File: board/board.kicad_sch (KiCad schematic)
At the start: 10 parts, among them U1 RP2040, U2 W25Q128JVS

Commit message: DVDD
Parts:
- added C10, C9: 100nF, Capacitor_SMD:C_0402_1005Metric, symbol Device:C_Small
- added C11: 1uF, Capacitor_SMD:C_0402_1005Metric, symbol Device:C_Small
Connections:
- net GND: now also C10.2, C11.2, C9.2
- net +1V1: now reaches U1.23 (DVDD), U1.50 (DVDD)
- net +1V1: now also U1.45 (VREG_VOUT), C10.1, C11.1, C9.1
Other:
- moved on the sheet: C8

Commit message: Flash
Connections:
- net +3V3: now also U2.8 (VCC)
- net GND: now also U2.4 (GND)
- net at U2.1 (~{CS}): now also U1.56 (QSPI_SS)
- net at U2.2 (DO(IO1)): now also U1.55 (QSPI_SD1)
- net at U2.3 (IO2): now also U1.54 (QSPI_SD2)
- net at U2.5 (DI(IO0)): now also U1.53 (QSPI_SD0)
- net at U2.6 (CLK): now also U1.52 (QSPI_SCLK)
- net at U2.7 (IO3): now also U1.51 (QSPI_SD3)
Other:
- moved on the sheet: U2
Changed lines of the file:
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@@
+	(wire
+		(pts
+			(xy 63.5 72.39) (xy 44.45 72.39)
+		)
+		(stroke
+			(width 0)
+			(type default)
+		)
+	)
 	(wire
 		(pts
@@
 	(wire
 		(pts
+			(xy 34.29 59.69) (xy 34.29 64.77)
+		)
+		(stroke
+			(width 0)
+			(type default)
+		)
+	)
+	(wire
+		(pts
 			(xy 54.61 27.94) (xy 54.61 29.21)
 		)
@@
 	(wire
 		(pts
+			(xy 44.45 80.01) (xy 64.77 80.01)
+		)
+		(stroke
+			(width 0)
+			(type default)
+		)
+	)
+	(wire
+		(pts
 			(xy 64.77 27.94) (xy 54.61 27.94)
 		)
@@
 	(wire
 		(pts
+			(xy 34.29 90.17) (xy 34.29 92.71)
+		)
+		(stroke
+			(width 0)
+			(type default)
+		)
+	)
+	(wire
+		(pts
 			(xy 100.33 29.21) (xy 104.14 29.21)
 		)
@@
 	(wire
 		(pts
+			(xy 64.77 85.09) (xy 63.5 85.09)
+		)
+		(stroke
+			(width 0)
+			(type default)
+		)
+	)
+	(wire
+		(pts
 			(xy 95.25 29.21) (xy 95.25 44.45)
 		)
@@
 	(wire
 		(pts
+			(xy 44.45 69.85) (xy 64.77 69.85)
+		)
+		(stroke
+			(width 0)
+			(type default)
+		)
+	)
+	(wire
+		(pts
 			(xy 101.6 20.32) (xy 104.14 20.32)
 		)
@@
 	(wire
 		(pts
+			(xy 44.45 77.47) (xy 64.77 77.47)
+		)
+		(stroke
+			(width 0)
+			(type default)
+		)
+	)
+	(wire
+		(pts
+			(xy 44.45 74.93) (xy 64.77 74.93)
+		)
+		(stroke
+			(width 0)
+			(type default)
+		)
+	)
+	(wire
+		(pts
 			(xy 161.29 29.21) (xy 172.72 29.21)
 		)
@@
 		(pts
 			(xy 149.86 24.13) (xy 161.29 24.13)
+		)
+		(stroke
+			(width 0)
+			(type default)
+		)
+	)
+	(wire
+		(pts
+			(xy 63.5 85.09) (xy 63.5 72.39)
+		)
+		(stroke
+			(width 0)
+			(type default)
+		)
+	)
+	(wire
+		(pts
+			(xy 44.45 82.55) (xy 64.77 82.55)
 		)
 		(stroke
@@
 	)
 	(symbol
+		(lib_id "power:GND")
+		(at 34.29 92.71 0)
+		(unit 1)
+		(exclude_from_sim no)
+		(in_bom yes)
+		(on_board yes)
+		(dnp no)
+		(property "Reference" "#PWR08"
+			(at 34.29 99.06 0)
+			(effects
+				(font
+					(size 1.27 1.27)
+				)
+				(hide yes)
+			)
+		)
+		(property "Value" "GND"
+			(at 37.592 94.488 0)
+			(effects
+				(font
+					(size 1.27 1.27)
+				)
+			)
+		)
+		(property "Footprint" ""
+			(at 34.29 92.71 0)
+			(effects
+				(font
+					(size 1.27 1.27)
+				)
+				(hide yes)
+			)
+		)
+		(property "Datasheet" ""
+			(at 34.29 92.71 0)
+			(effects
+				(font
+					(size 1.27 1.27)
+				)
+				(hide yes)
+			)
+		)
+		(property "Description" "Power symbol creates a global label with name \"GND\" , ground"
+			(at 34.29 92.71 0)
+			(effects
+				(font
+					(size 1.27 1.27)
+				)
+				(hide yes)
+			)
+		)
+		(pin "1"
+		)
+		(instances
+			(project "board"
+				(path "/6eb10beb-f31c-4c13-8f79-f4b6753787bf"
+					(reference "#PWR08")
+					(unit 1)
+				)
+			)
+		)
+	)
+	(symbol
 		(lib_id "Device:C_Small")
 		(at 64.77 39.37 0)
@@
 	(symbol
 		(lib_id "Memory_Flash:W25Q128JVS")
-		(at 160.02 54.61 0)
+		(at 34.29 77.47 0)
+		(mirror y)
 		(unit 1)
 		(exclude_from_sim no)
@@
 		(on_board yes)
 		(dnp no)
-		(fields_autoplaced yes)
 		(property "Reference" "U2"
-			(at 168.91 53.3399 0)
+			(at 25.4 76.1999 0)
 			(effects
 				(font
@@
 		)
 		(property "Value" "W25Q128JVS"
-			(at 168.91 55.8799 0)
+			(at 25.4 78.7399 0)
 			(effects
 				(font
@@
 		)
 		(property "Footprint" "Package_SO:SOIC-8_5.23x5.23mm_P1.27mm"
-			(at 160.02 54.61 0)
+			(at 34.29 77.47 0)
 			(effects
 				(font
@@
 		)
 		(property "Datasheet" "http://www.winbond.com/resource-files/w25q128jv_dtr%20revc%2003272018%20plus.pdf"
-			(at 160.02 54.61 0)
+			(at 34.29 77.47 0)
 			(effects
 				(font
@@
 		)
 		(property "Description" "128Mb Serial Flash Memory, Standard/Dual/Quad SPI, SOIC-8"
-			(at 160.02 54.61 0)
+			(at 34.29 77.47 0)
 			(effects
 				(font
@@
 					(unit 1)
 				)
+			)
+		)
+	)
+	(symbol
+		(lib_id "power:VCC")
+		(at 34.29 59.69 0)
+		(unit 1)
+		(exclude_from_sim no)
+		(in_bom yes)
+		(on_board yes)
+		(dnp no)
+		(property "Reference" "#PWR07"
+			(at 34.29 63.5 0)
+			(effects
+				(font
+					(size 1.27 1.27)
+				)
+				(hide yes)
+			)
+		)
+		(property "Value" "+3V3"
+			(at 34.29 54.102 0)
+			(effects
+				(font
+					(size 1.27 1.27)
+				)
+			)
+		)
+		(property "Footprint" ""
+			(at 34.29 59.69 0)
+			(effects
+				(font
+					(size 1.27 1.27)
+				)
+				(hide yes)
+			)
+		)
+		(property "Datasheet" ""
+			(at 34.29 59.69 0)
+			(effects
+				(font
+					(size 1.27 1.27)
+				)
+				(hide yes)
+			)
+		)
+		(property "Description" "Power symbol creates a global label with name \"VCC\""
+			(at 34.29 59.69 0)
+			(effects
+				(font
+					(size 1.27 1.27)
+				)
+				(hide yes)
+			)
+		)
+		(pin "1"
+		)
+		(instances
+			(project "board"
+				(path "/6eb10beb-f31c-4c13-8f79-f4b6753787bf"
+					(reference "#PWR07")
+					(unit 1)
+				)

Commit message: USB hopefully
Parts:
- added P1: USB_C_Plug_USB2.0, symbol Connector:USB_C_Plug_USB2.0
- added R1, R2: 27.4, symbol Device:R_Small
- added R3: 5.1k, symbol Device:R_Small
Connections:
- net GND: now also U1.19 (TESTEN), U1.57 (GND), P1.A1 (GND), P1.A12 (GND), P1.B1 (GND), P1.B12 (GND), P1.S1 (SHIELD), R3.2
- net at U1.46 (USB_DM): now also R1.2
- net at U1.47 (USB_DP): now also R2.2
- new net: P1.A5 (CC), R3.1
- new net: P1.A6 (D+), R2.1
- new net: P1.A7 (D-), R1.1
- new net VBUS: P1.A4 (VBUS), P1.A9 (VBUS), P1.B4 (VBUS), P1.B9 (VBUS)

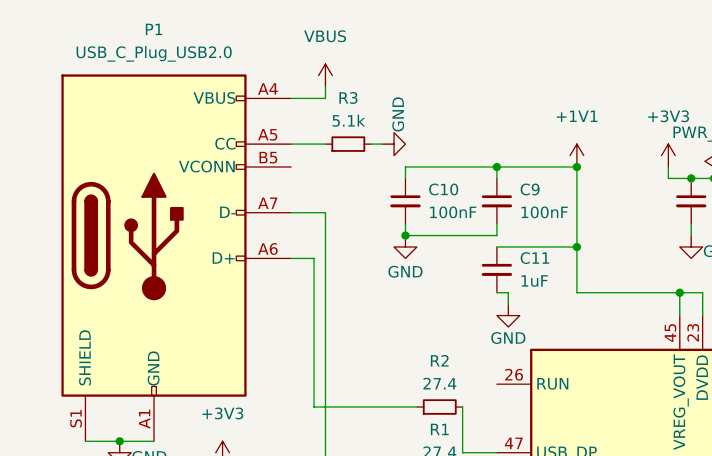
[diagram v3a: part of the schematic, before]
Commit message: implement proper usb C
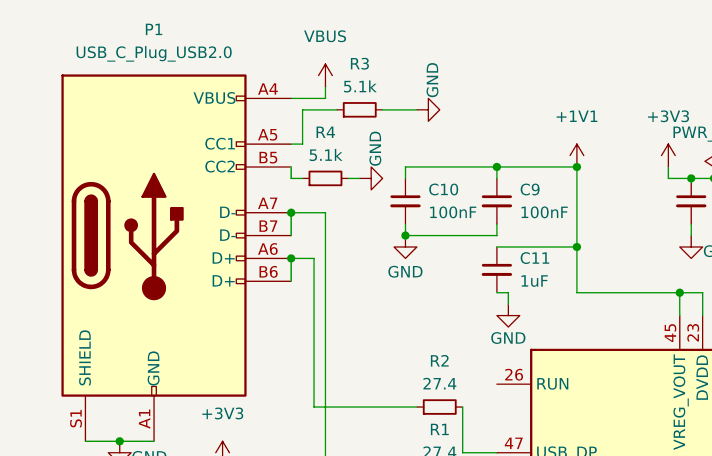
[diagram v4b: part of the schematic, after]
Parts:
- added R4: 5.1k, Resistor_SMD:R_0402_1005Metric, symbol Device:R_Small
- P1: footprint (none) -> Connector_USB:USB_C_Receptacle_G-Switch_GT-USB-7010ASV; symbol Connector:USB_C_Plug_USB2.0 -> Connector:USB_C_Receptacle_USB2.0_14P
- R1, R2, R3: footprint (none) -> Resistor_SMD:R_0402_1005Metric
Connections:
- net GND: now also R4.2
- net at P1.A6 (D+), R2.1: now also P1.B6 (D+)
- net at P1.A7 (D-), R1.1: now also P1.B7 (D-)
- net at P1.B5 (CC2): now also R4.1
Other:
- moved on the sheet: R3

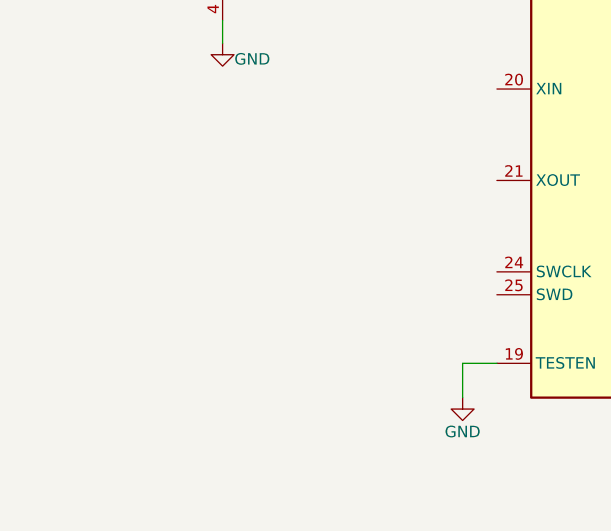
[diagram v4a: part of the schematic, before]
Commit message: voltage regulator
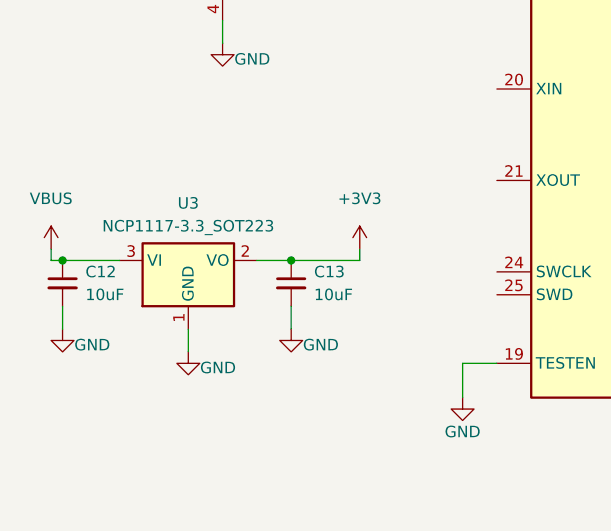
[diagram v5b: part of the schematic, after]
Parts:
- added C12, C13: 10uF, Capacitor_SMD:C_0402_1005Metric, symbol Device:C_Small
- added U3: NCP1117-3.3_SOT223, Package_TO_SOT_SMD:SOT-223-3_TabPin2, symbol Regulator_Linear:NCP1117-3.3_SOT223
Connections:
- net +3V3: now also C13.1, U3.2 (VO)
- net GND: now also C12.2, C13.2, U3.1 (GND)
- net VBUS: now also C12.1, U3.3 (VI)

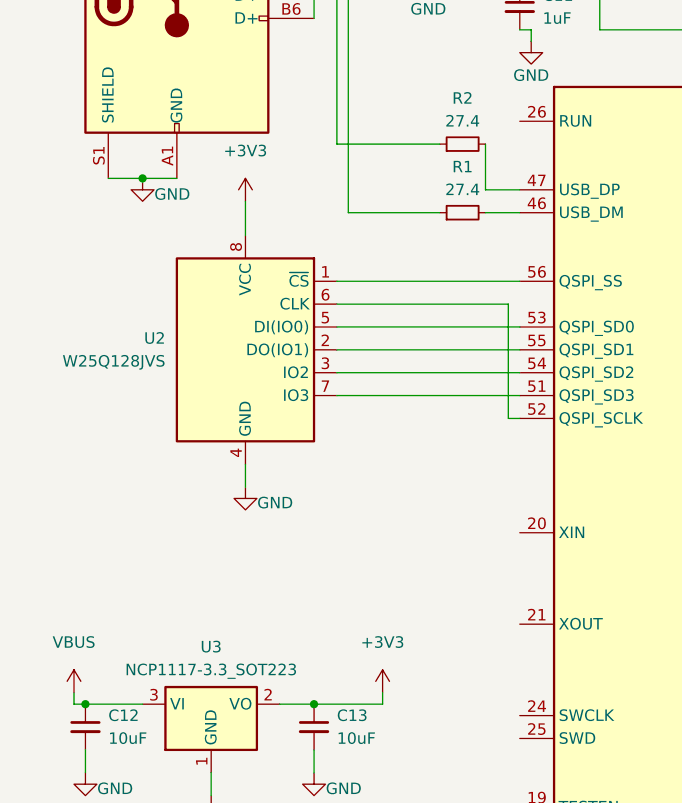
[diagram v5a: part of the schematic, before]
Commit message: flash resistors and BOOTSEL button
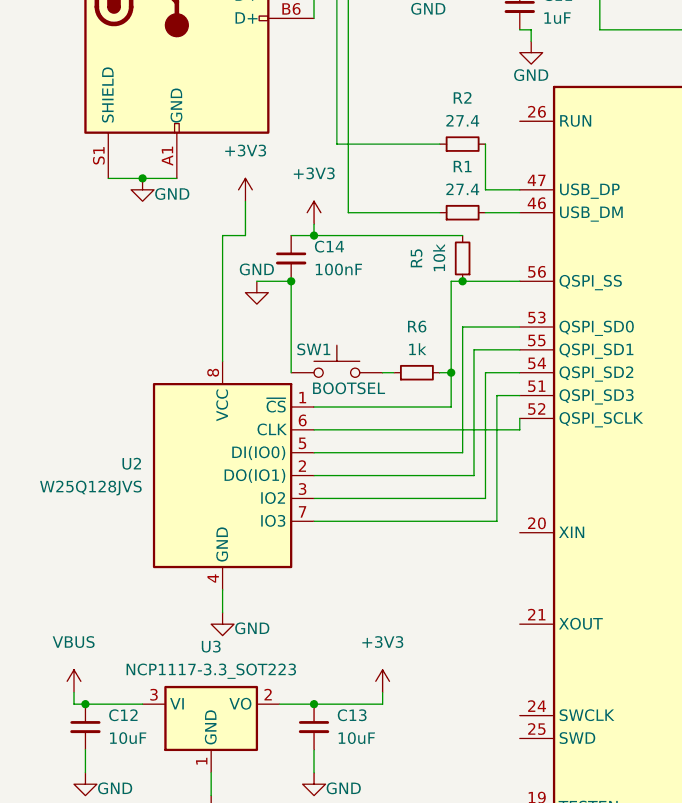
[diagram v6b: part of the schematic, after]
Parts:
- added C14: 100nF, Capacitor_SMD:C_0402_1005Metric, symbol Device:C_Small
- added R5: 10k, Resistor_SMD:R_0402_1005Metric, symbol Device:R_Small
- added R6: 1k, Resistor_SMD:R_0402_1005Metric, symbol Device:R_Small
- added SW1: BOOTSEL, Button_Switch_SMD:SW_Push_SPST_NO_Alps_SKRK, symbol Switch:SW_Push
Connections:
- net +3V3: now also C14.1, R5.2
- net GND: now also C14.2, SW1.1
- net at U1.56 (QSPI_SS), U2.1 (~{CS}): now also R5.1, R6.2
- new net: R6.1, SW1.2
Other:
- moved on the sheet: U2

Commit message: crystal oscillator
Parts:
- added C15, C16: 15pF, Capacitor_SMD:C_0402_1005Metric, symbol Device:C_Small
- added R7: 1k, Resistor_SMD:R_0402_1005Metric, symbol Device:R_Small
- added Y1: ABM8-272-T3, symbol Device:Crystal_GND24
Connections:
- net GND: now also C15.1, C16.1, Y1.2, Y1.4
- net at U1.20 (XIN): now also C16.2, Y1.3
- net at U1.21 (XOUT): now also R7.2
- new net: C15.2, R7.1, Y1.1

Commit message: crystal footprint
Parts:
- Y1: footprint (none) -> personal:ABM8-272-T3_ABR
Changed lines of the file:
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@@
 			)
 		)
-		(property "Footprint" ""
+		(property "Footprint" "personal:ABM8-272-T3_ABR"
 			(at 31.75 139.7 0)
 			(effects
